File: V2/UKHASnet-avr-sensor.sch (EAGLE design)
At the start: 33 parts, among them J1 AVR_SPI_PRG_62X3_LOCK, U1 MCP1700-3302E/TO, U2 ATMEGA328P-PU, X1 SMA-142-0711-881/886, Y1 RESONATORPTH

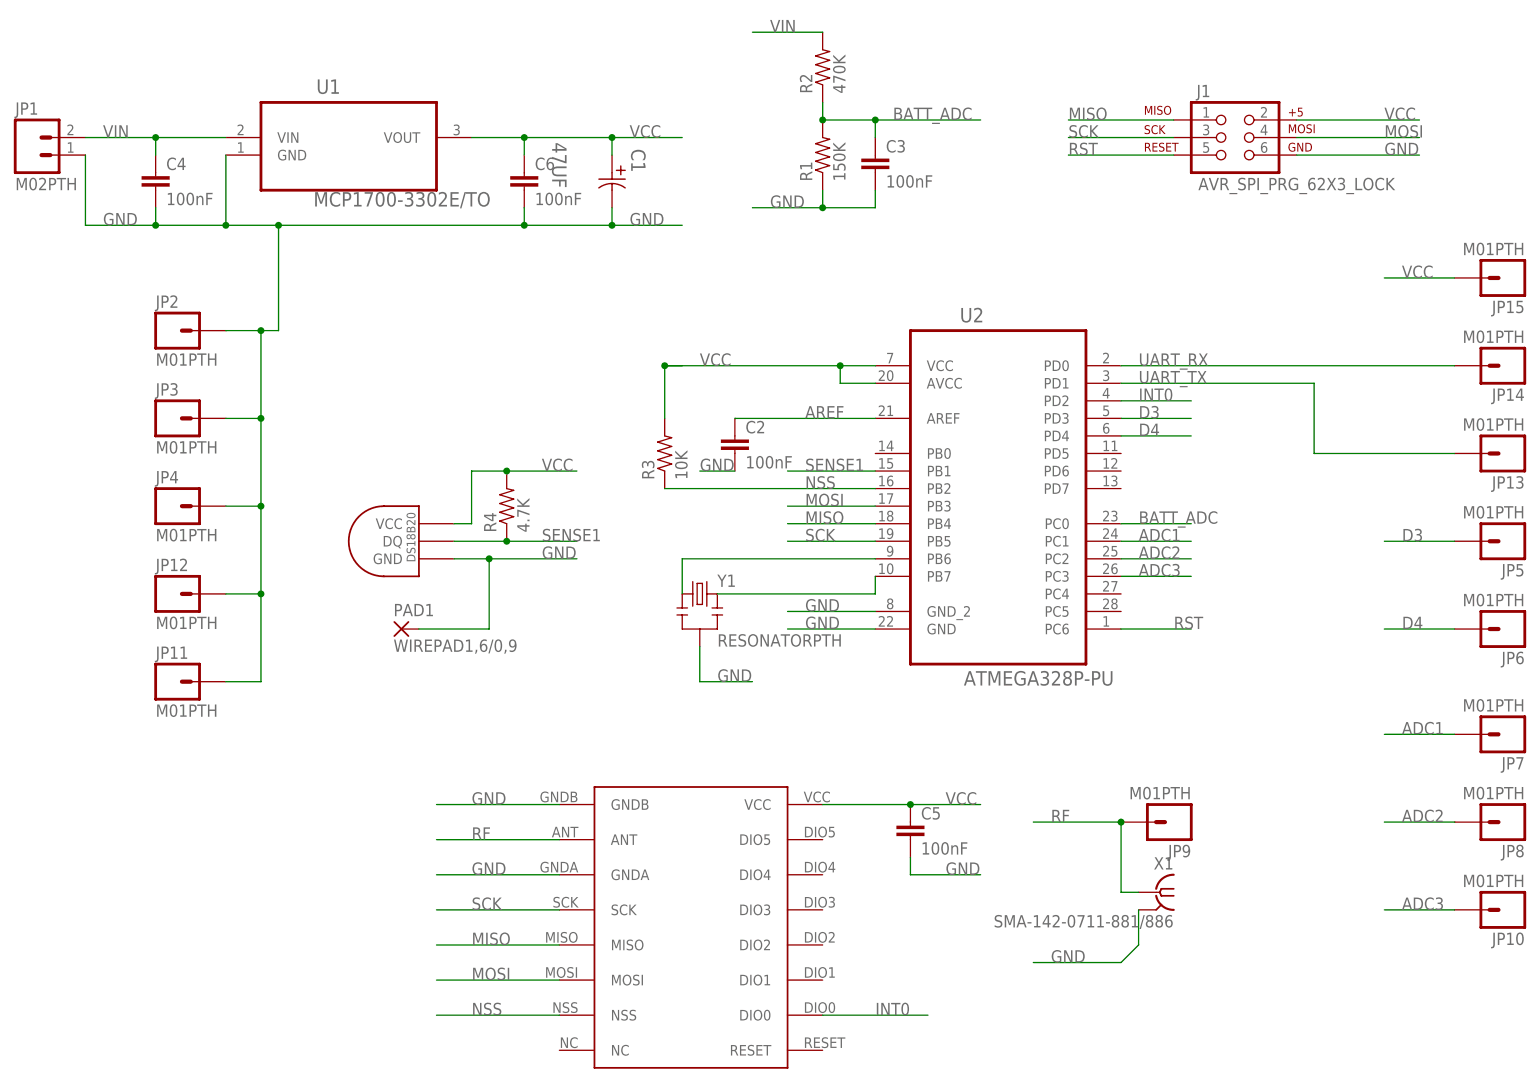
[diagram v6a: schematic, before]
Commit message: Silkscreen changes.
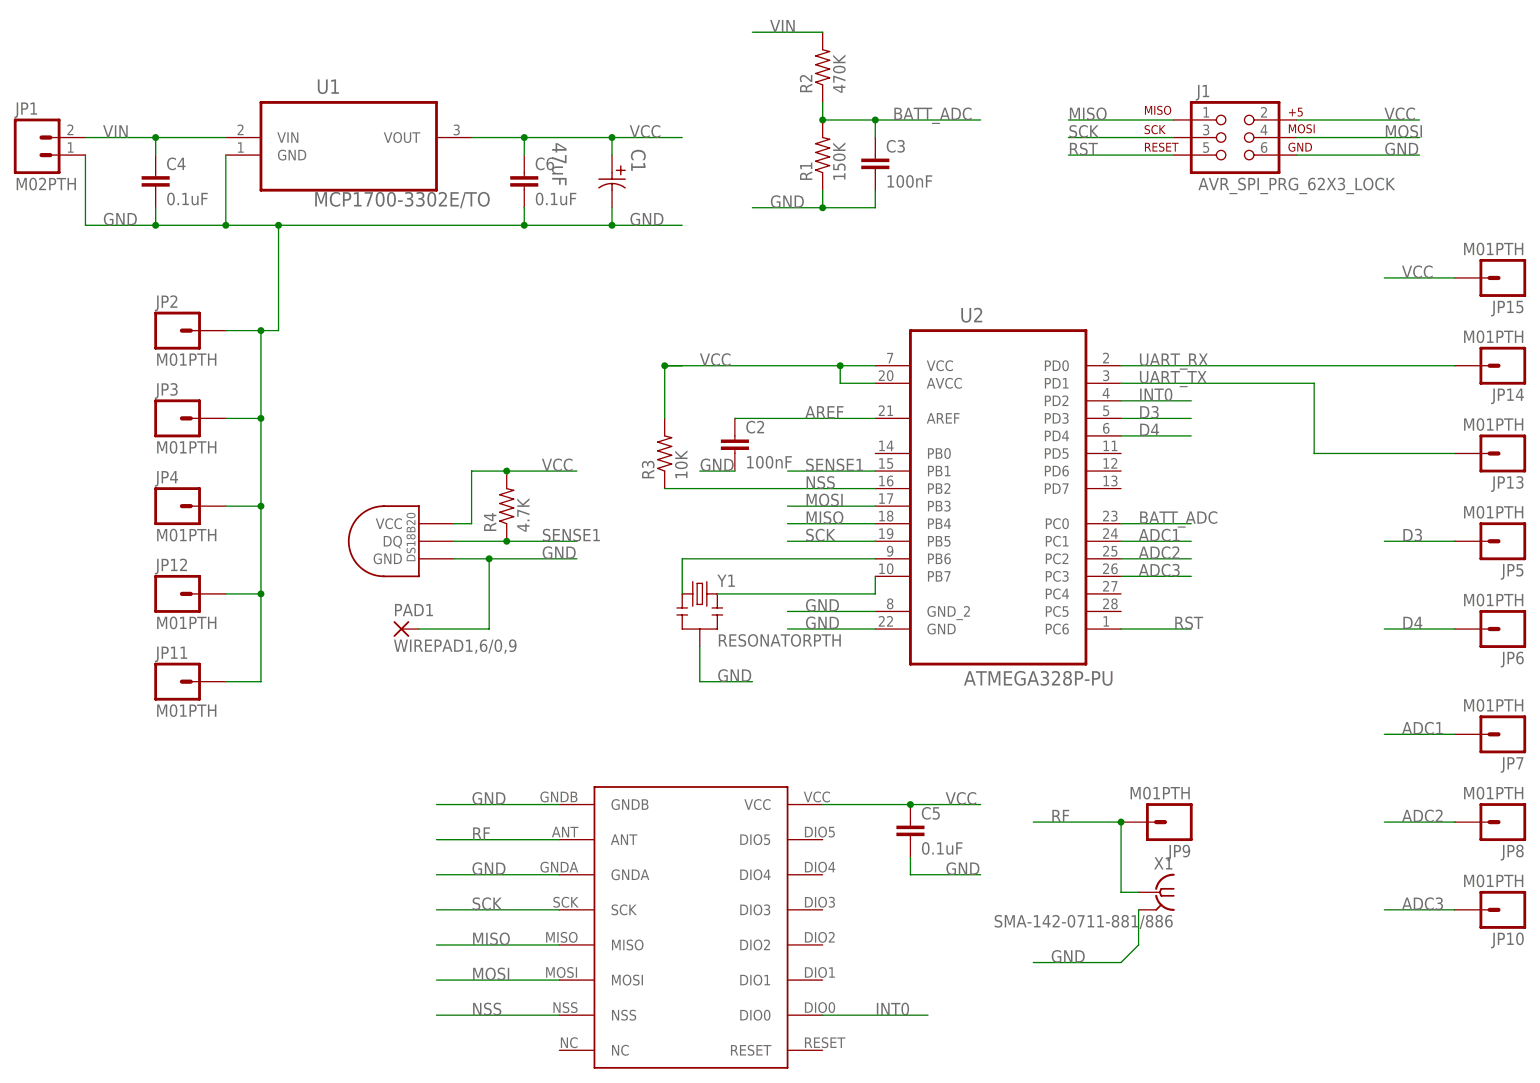
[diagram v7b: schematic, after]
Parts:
- C1: value 47UF -> 47uF
- C4, C5, C6: value 100nF -> 0.1uF
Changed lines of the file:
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@@
 <part name="R2" library="SparkFun" deviceset="RESISTOR" device="PTH-1/4W" value="470K"/>
 <part name="R3" library="SparkFun" deviceset="RESISTOR" device="PTH-1/4W" value="10K"/>
-<part name="C1" library="1000ufCap" deviceset="EEU" device="-P1.5" technology="FC1J6R8" value="47UF"/>
+<part name="C1" library="1000ufCap" deviceset="EEU" device="-P1.5" technology="FC1J6R8" value="47uF"/>
 <part name="R4" library="SparkFun" deviceset="RESISTOR" device="PTH-1/4W" value="4.7K"/>
 <part name="Y1" library="SparkFun" deviceset="RESONATOR" device="PTH"/>
@@
 <part name="C2" library="capacitor-wima" deviceset="C" device="2.5/2" value="100nF"/>
 <part name="C3" library="capacitor-wima" deviceset="C" device="2.5/2" value="100nF"/>
-<part name="C4" library="capacitor-wima" deviceset="C" device="2.5/2" value="100nF"/>
-<part name="C6" library="capacitor-wima" deviceset="C" device="2.5/2" value="100nF"/>
-<part name="C5" library="capacitor-wima" deviceset="C" device="2.5/2" value="100nF"/>
+<part name="C4" library="capacitor-wima" deviceset="C" device="2.5/2" value="0.1uF"/>
+<part name="C6" library="capacitor-wima" deviceset="C" device="2.5/2" value="0.1uF"/>
+<part name="C5" library="capacitor-wima" deviceset="C" device="2.5/2" value="0.1uF"/>
 <part name="JP5" library="SparkFun-Connectors" deviceset="M01" device="PTH"/>
 <part name="JP6" library="SparkFun-Connectors" deviceset="M01" device="PTH"/>

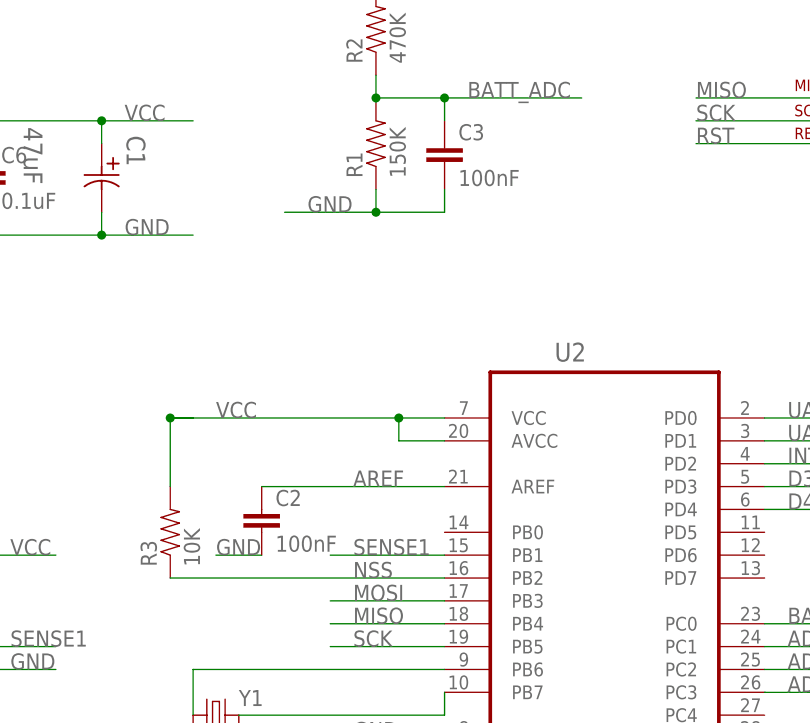
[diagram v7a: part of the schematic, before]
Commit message: Silkscreen changes.
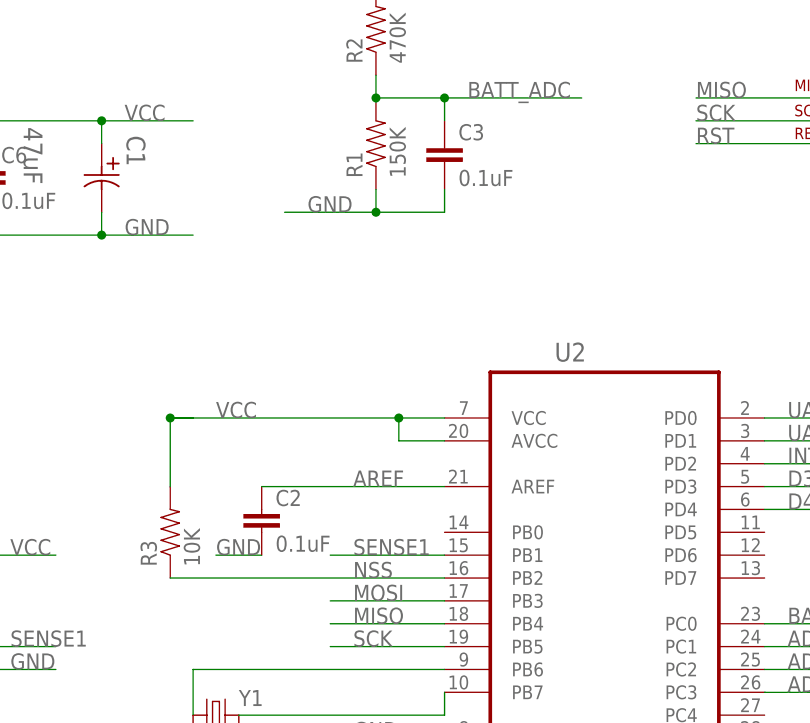
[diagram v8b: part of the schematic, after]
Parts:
- C2, C3: value 100nF -> 0.1uF
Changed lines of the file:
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@@
 <part name="JP13" library="SparkFun-Connectors" deviceset="M01" device="PTH"/>
 <part name="JP14" library="SparkFun-Connectors" deviceset="M01" device="PTH"/>
-<part name="C2" library="capacitor-wima" deviceset="C" device="2.5/2" value="100nF"/>
-<part name="C3" library="capacitor-wima" deviceset="C" device="2.5/2" value="100nF"/>
+<part name="C2" library="capacitor-wima" deviceset="C" device="2.5/2" value="0.1uF"/>
+<part name="C3" library="capacitor-wima" deviceset="C" device="2.5/2" value="0.1uF"/>
 <part name="C4" library="capacitor-wima" deviceset="C" device="2.5/2" value="0.1uF"/>
 <part name="C6" library="capacitor-wima" deviceset="C" device="2.5/2" value="0.1uF"/>
